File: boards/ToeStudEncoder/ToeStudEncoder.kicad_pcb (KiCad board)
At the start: 2 copper layers, 95 x 57.4 mm, 26 parts, among them J1 Swell, J2 ISP, J3 ToeLeft, J4 ToeRight, J5 MIDI In, J8 MIDI Out, J9 Controller, U1 ATmega48-20P, U2 6N137, U3 L7805

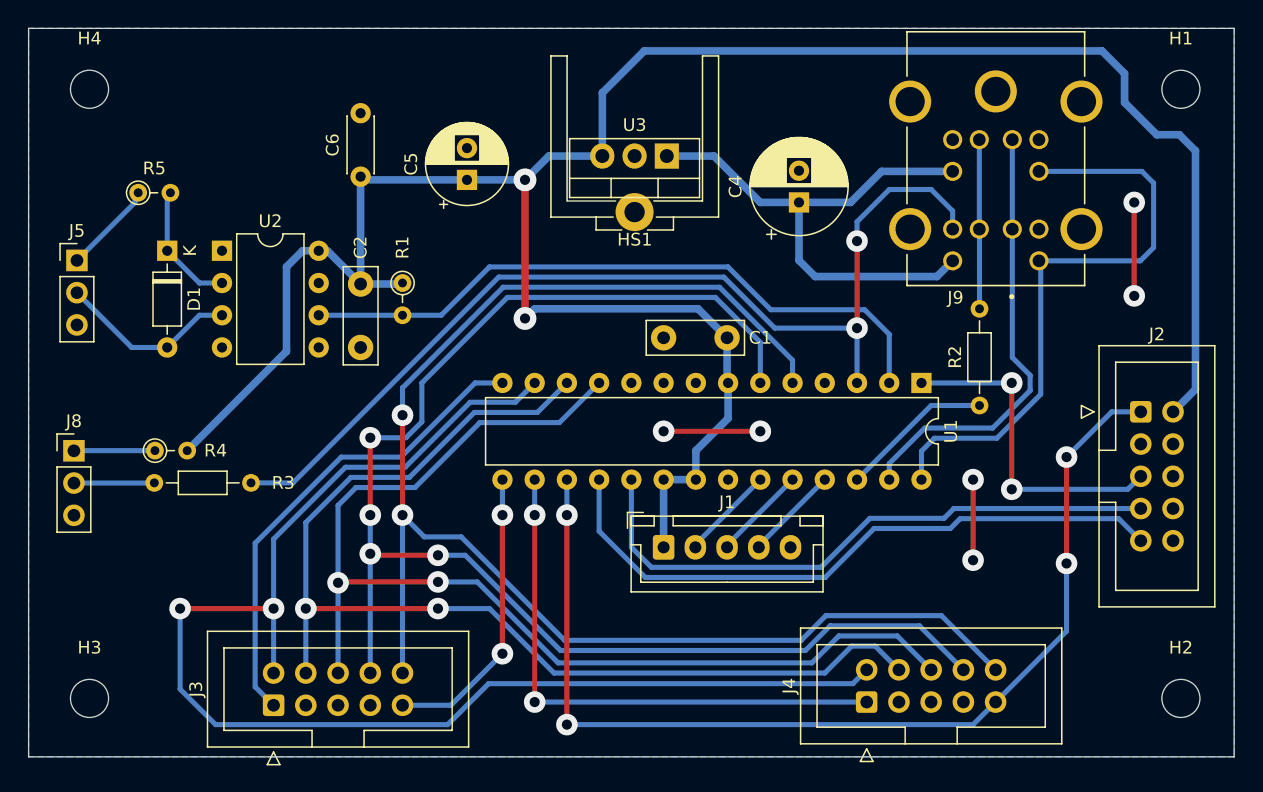
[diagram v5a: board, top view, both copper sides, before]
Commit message: Cleanup of PCB sizes and mounthole positions. Moved MIDI connectors to separate board.
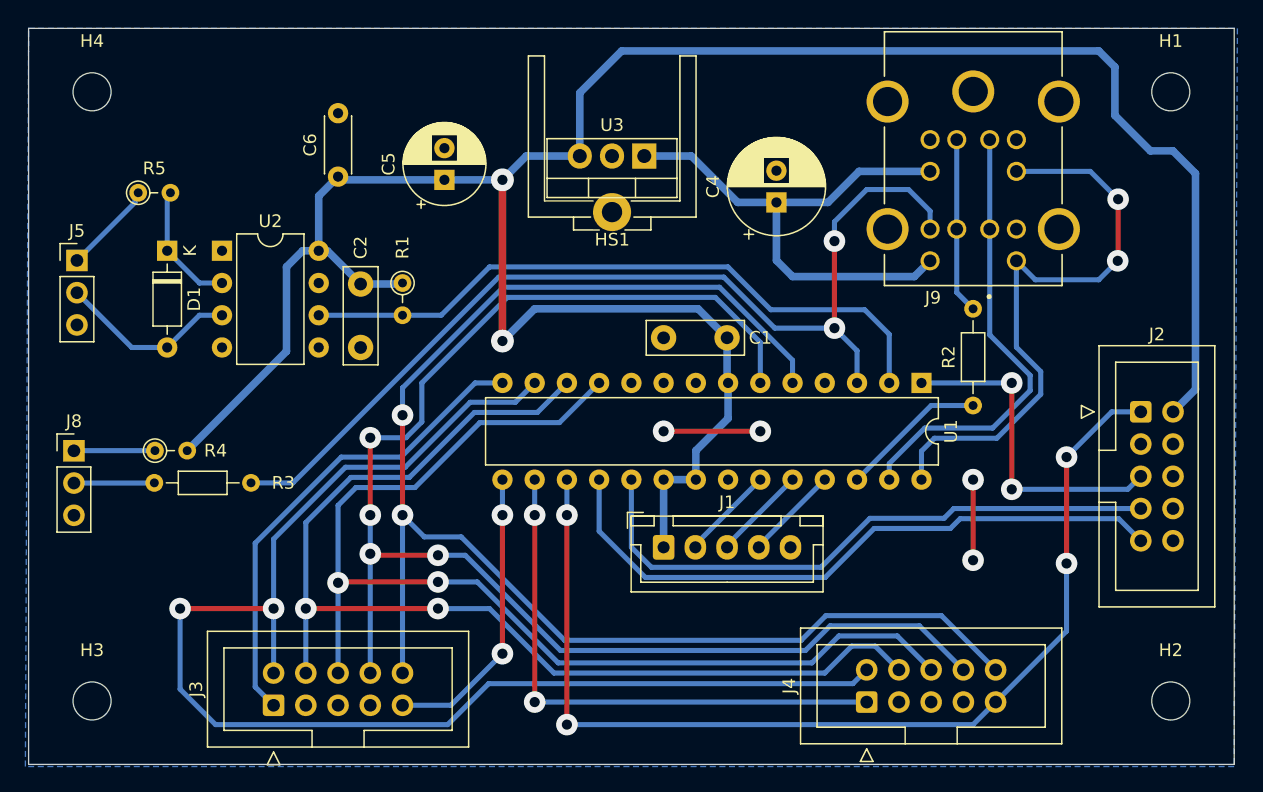
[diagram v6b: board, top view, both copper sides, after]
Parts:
- moved C4 1.78 mm to (169.2, 65.8)
- moved U3 1.78 mm to (158.7, 62.1)
- moved C5 1.78 mm to (143.0, 64.0)
- moved C6 1.78 mm to (134.6, 63.8)
- moved HS1 1.78 mm to (156.2, 65.7)
- moved J9 1.78 mm to (184.7, 52.3)
- moved H1 0.82 mm to (200.2, 57.1)
- moved H2 0.82 mm to (200.2, 105.1)
- moved R2 0.51 mm to (184.7, 81.8)
- moved H4 0.28 mm to (115.2, 57.1)
- moved H3 0.28 mm to (115.2, 105.1)
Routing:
- net GND: track 21.3 -> 14.0 mm, vias 6 -> 4
- net +5V: track 184.0 -> 187.7 mm
- net TXD: track 79.3 -> 78.5 mm
- net SDA: track 35.1 -> 35.8 mm
- net Net-(J9-Pad2_1): track 13.3 -> 13.9 mm
- net SCL: vias 0 -> 2
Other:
- board size 95 x 57.4 mm -> 95 x 58 mm

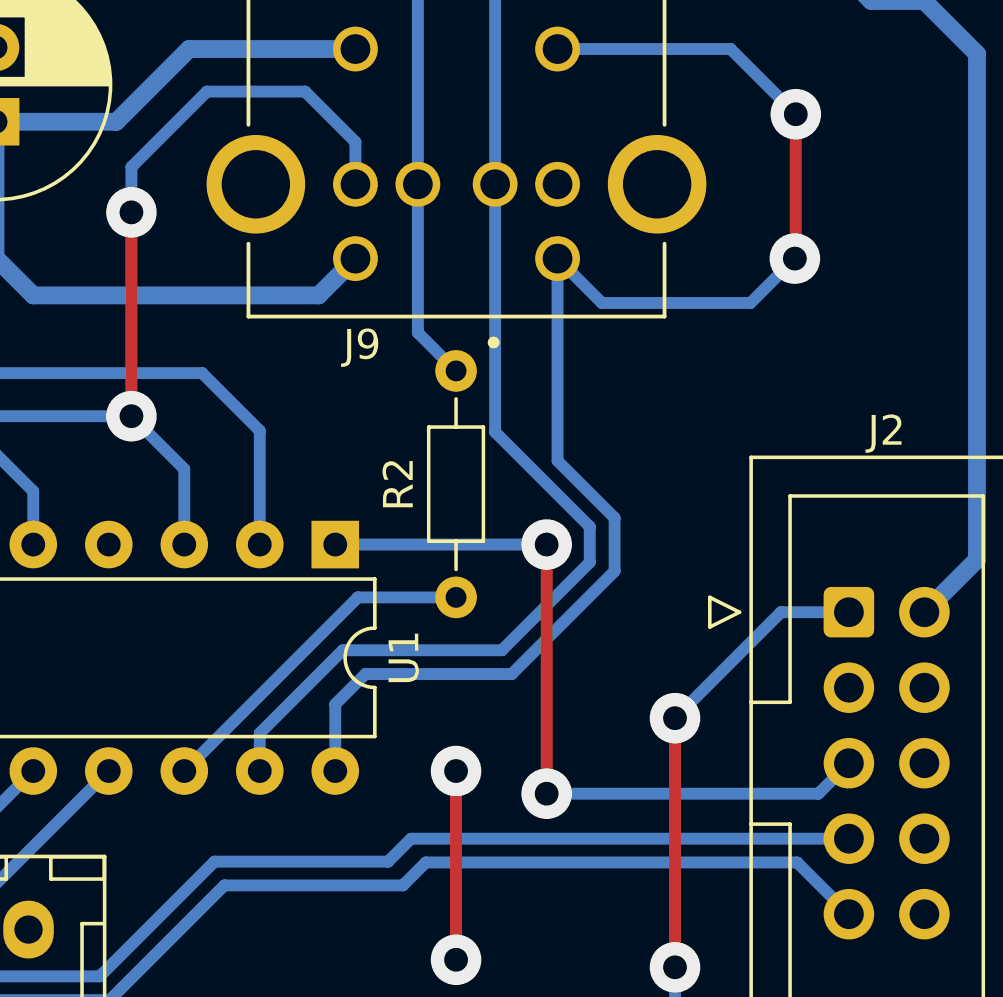
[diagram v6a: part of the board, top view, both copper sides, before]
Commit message: Fixed interrupt line to use open collector, added pullups to I2C lines
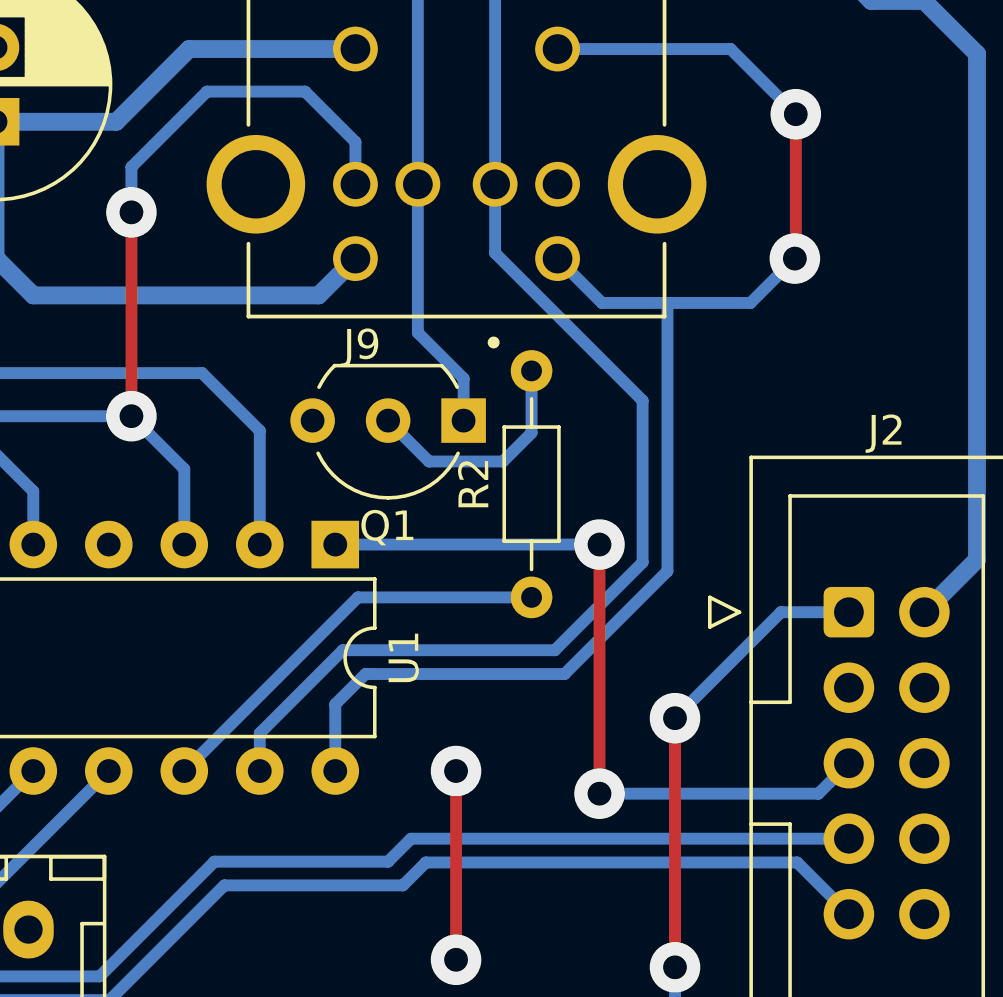
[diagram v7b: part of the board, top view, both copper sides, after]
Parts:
- added Q1: BC547, Package_TO_SOT_THT:TO-92_Inline_Wide, F.Cu at (184.9, 75.8)
- R1: value 1k -> 10k
- R2: value 220 -> 4k7
- moved R2 2.54 mm to (187.2, 81.8)
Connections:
- J9 pad 2_1: Net-(J9-Pad2_1) -> Net-(Q1-C)
- J9 pad 2_2: Net-(J9-Pad2_1) -> Net-(Q1-C)
- R2 pad 2: Net-(J9-Pad2_1) -> Net-(Q1-B)
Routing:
- net Net-(Q1-C): track 0.00 -> 15.6 mm
- net Net-(J9-Pad2_1): track 13.9 -> 0.00 mm
- net Net-(Q1-B): track 0.00 -> 7.88 mm
- net SDA: track 35.8 -> 38.4 mm
- net Interrupt: track 12.1 -> 14.1 mm
- net SCL: track 47.8 -> 47.3 mm

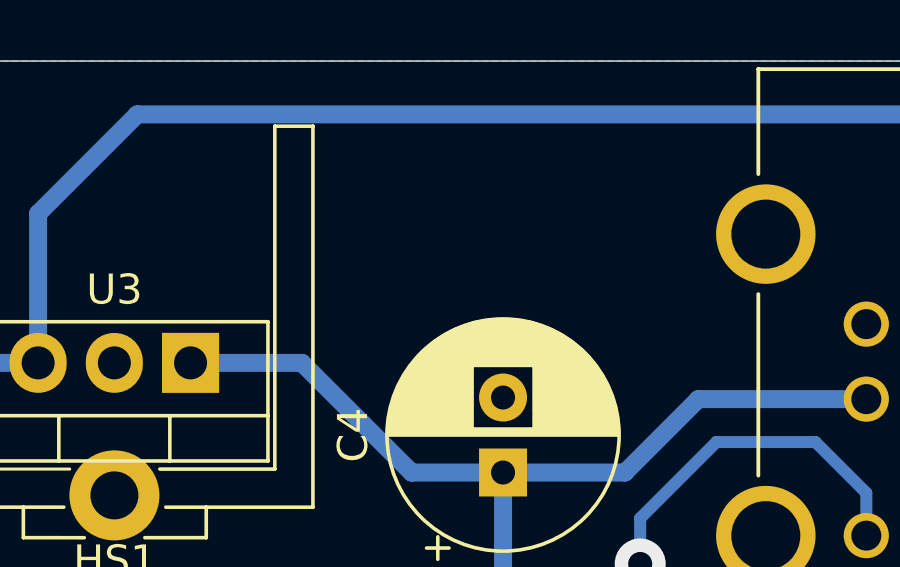
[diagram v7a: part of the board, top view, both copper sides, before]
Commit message: Added bypass caps to power supplies, use cheaper MAX232 IC.
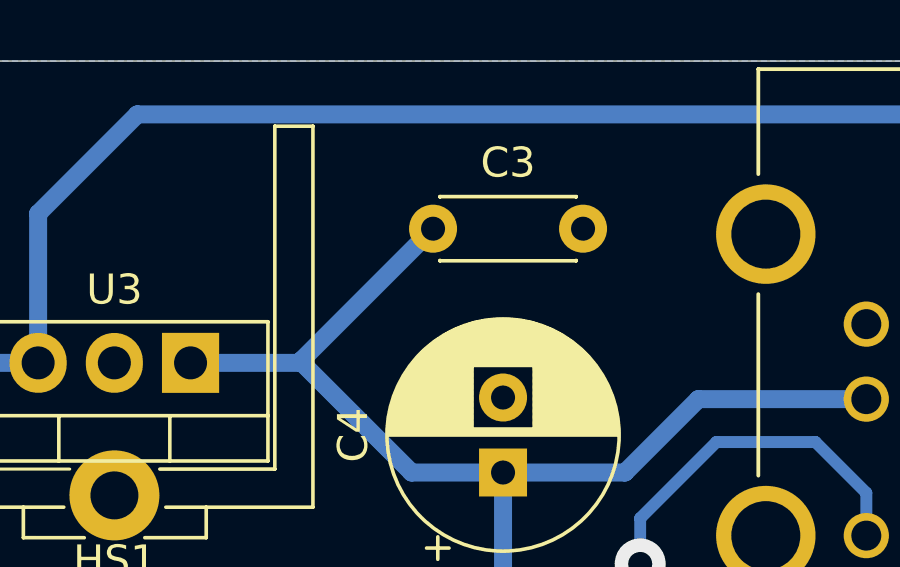
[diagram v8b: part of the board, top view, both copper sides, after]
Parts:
- added C3: 330nF, Capacitor_THT:C_Disc_D4.3mm_W1.9mm_P5.00mm, F.Cu at (166.8, 57.7)
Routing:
- net +12V: track 42.8 -> 49.1 mm
